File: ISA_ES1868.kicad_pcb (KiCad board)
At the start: 4 copper layers, 104.1 x 102.9 mm, 107 parts, among them J1 LINE IN, J10 Volume buttons, J11 ISA BUS, J2 MIC, J3 Joystick/MIDI, J5 Wavetable, J7 SPKR OUT, J8 LINE OUT, U1 L78L05, U2 74LS138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

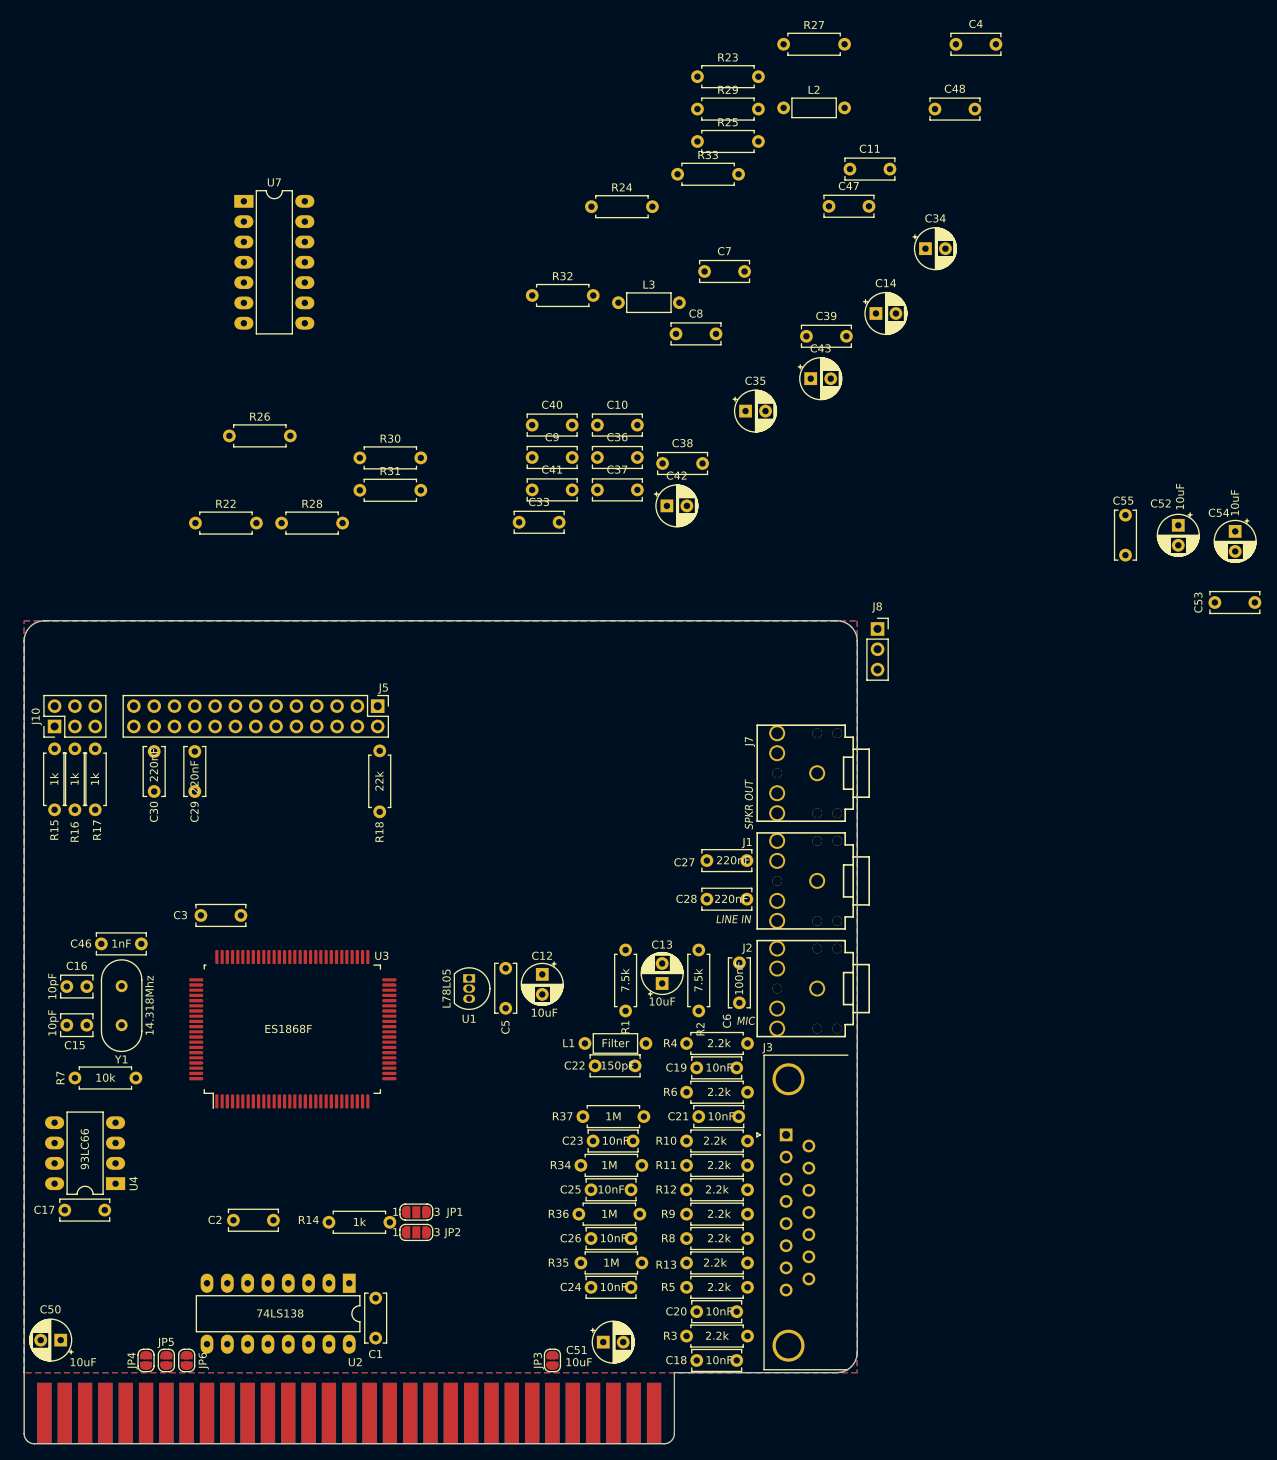
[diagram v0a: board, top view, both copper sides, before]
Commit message: Routed audio traces
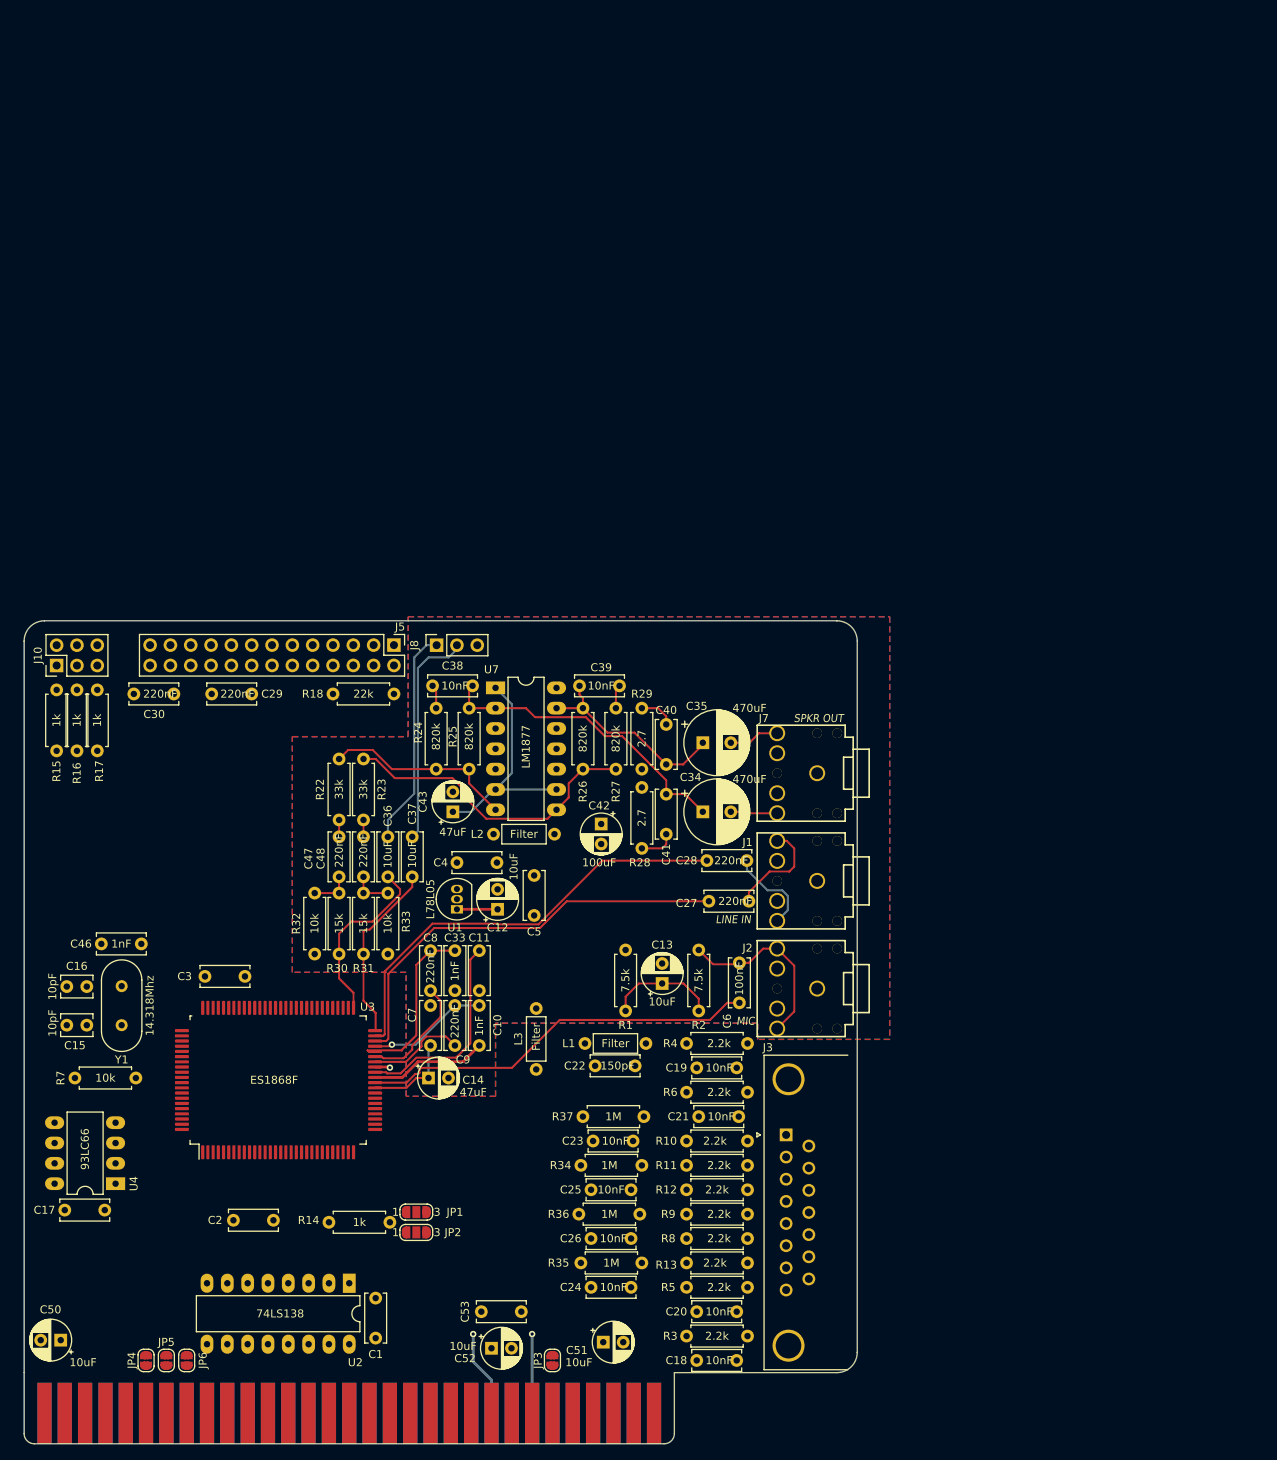
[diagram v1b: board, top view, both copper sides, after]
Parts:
- removed C54: 10uF, Capacitor_THT:CP_Radial_D5.0mm_P2.50mm
- removed C55: 100nF, Capacitor_THT:C_Disc_D6.0mm_W2.5mm_P5.00mm
- C34, C35: footprint Capacitor_THT:CP_Radial_D5.0mm_P2.50mm -> Capacitor_THT:CP_Radial_D8.0mm_P3.50mm
- L2, L3: value Ferrite Bead -> Filter
- moved C52 134.0 mm to (269.2, 191.3), turned to 0 degrees
- moved C53 127.5 mm to (268.0, 186.7)
- moved C4 119.8 mm to (264.9, 130.6)
- moved C48 119.6 mm to (253.2, 132.3), turned to 90 degrees
- moved C14 110.7 mm to (261.4, 157.5)
- moved C11 108.1 mm to (267.7, 141.6), turned to 270 degrees
- moved C47 103.8 mm to (250.2, 132.3), turned to 90 degrees
- moved C7 102.6 mm to (261.6, 153.4), turned to 90 degrees
- moved R23 101.9 mm to (253.2, 125.2), turned to 90 degrees
- moved L2 97.8 mm to (269.5, 127.0)
- moved R33 96.9 mm to (256.3, 134.4), turned to 270 degrees
- moved L3 96.4 mm to (274.8, 156.4), turned to 90 degrees
- moved R27 93.0 mm to (284.8, 118.9), turned to 90 degrees
- moved C8 87.6 mm to (261.6, 146.6), turned to 90 degrees
- moved R25 83.5 mm to (266.4, 118.9), turned to 90 degrees
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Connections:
- net Net-(C42-Pad1) renamed /Filtered_12V
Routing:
- net GNDA: track 0.00 -> 309.9 mm
- net +12V: track 0.00 -> 127.1 mm, vias 0 -> 1
- net Net-(C28-Pad1): track 0.00 -> 55.2 mm
- net Net-(C27-Pad1): track 0.00 -> 53.7 mm
- net Net-(C6-Pad1): track 0.00 -> 49.9 mm
- net /VDDA: track 0.00 -> 49.5 mm, vias 0 -> 1
- net Net-(R23-Pad2): track 0.00 -> 38.8 mm
- net Net-(C34-Pad1): track 0.00 -> 38.6 mm
- net Net-(C43-Pad1): track 0.00 -> 28.5 mm
- net Net-(C37-Pad2): track 0.00 -> 27.8 mm
- net Net-(C36-Pad2): track 0.00 -> 27.2 mm
- net /Filtered_12V: track 0.00 -> 27.2 mm
- net Net-(C11-Pad1): track 0.00 -> 26.4 mm
- net Net-(C35-Pad1): track 0.00 -> 25.4 mm
- net Net-(R22-Pad2): track 0.00 -> 24.2 mm
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- added copper zone on In2.Cu, net /VDDA
- added copper zone on B.Cu, net GNDA
- added copper zone on F.Cu, net GNDA
- added copper zone on In1.Cu, net GNDA
- removed copper zone on B.Cu, net GND
- removed copper zone on F.Cu, net GND

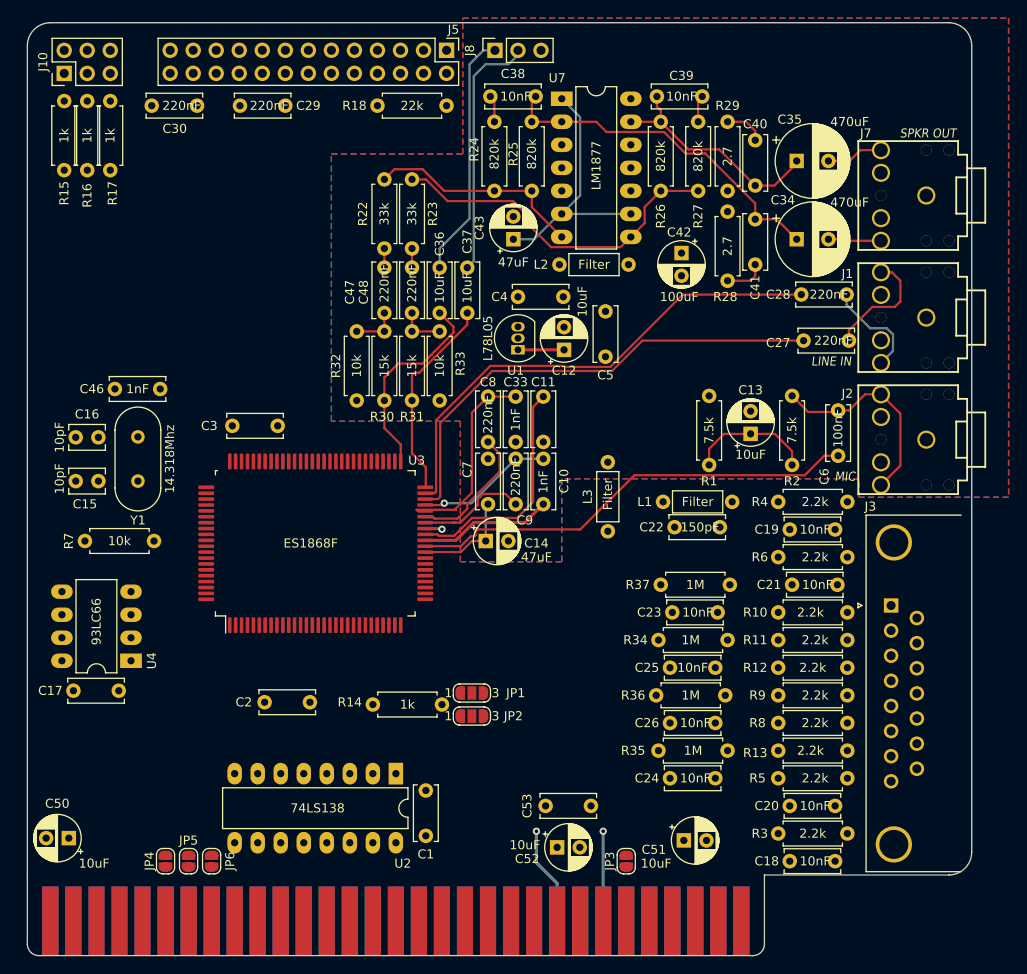
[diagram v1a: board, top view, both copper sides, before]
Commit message: Basic power routing
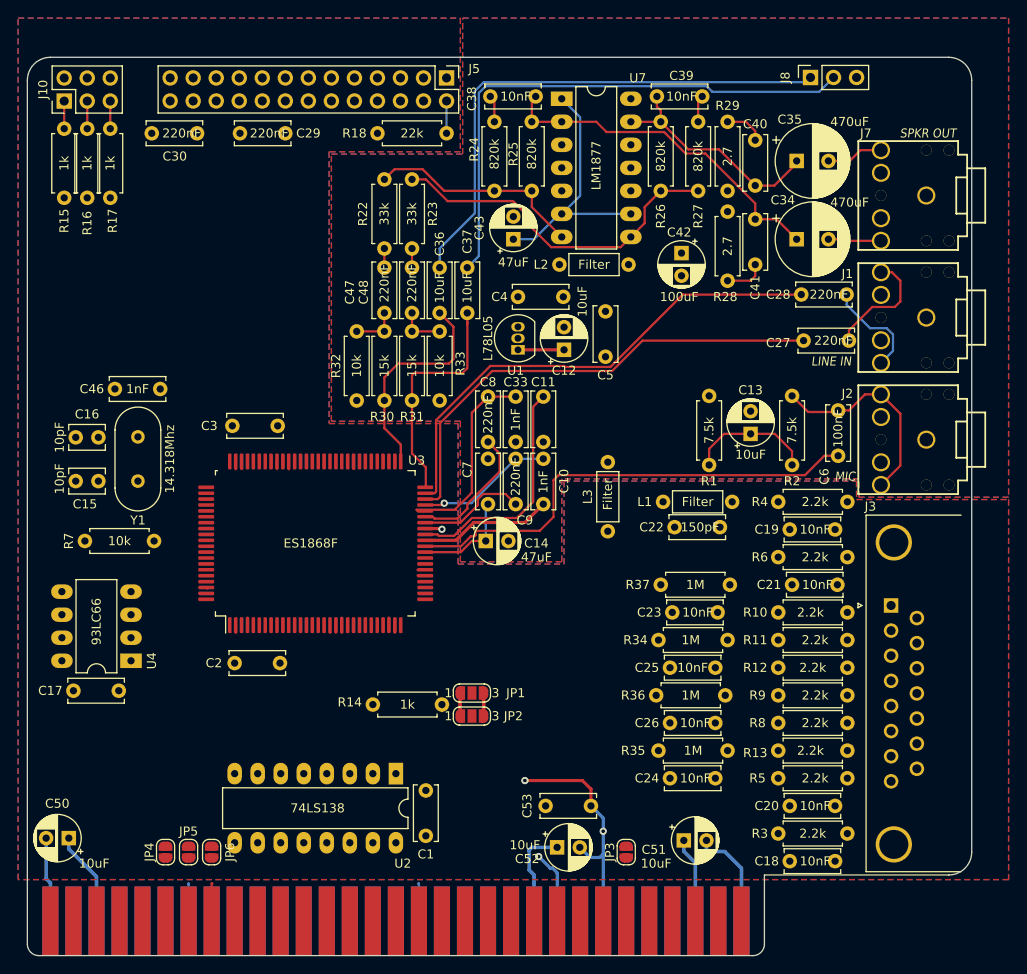
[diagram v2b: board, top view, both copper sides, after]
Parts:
- moved J8 34.9 mm to (297.2, 106.4)
- moved C2 5.44 mm to (233.7, 170.9)
- moved C29 3.05 mm to (239.3, 112.5)
- moved C30 3.05 mm to (224.5, 112.5)
- moved J5 3.05 mm to (257.0, 106.4)
- moved R15 3.05 mm to (214.9, 119.6)
- moved R16 3.05 mm to (217.4, 119.6)
- moved R17 3.05 mm to (220.0, 119.6)
- moved R18 3.05 mm to (257.0, 112.5)
- moved J10 3.05 mm to (214.9, 109.0)
- moved JP3 1.00 mm to (276.9, 191.8)
- moved JP4 1.00 mm to (226.1, 191.8)
- moved JP5 1.00 mm to (228.6, 191.8)
- moved JP6 1.00 mm to (231.1, 191.8)
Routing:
- net GND: track 0.00 -> 446.0 mm
- net VCC: track 0.00 -> 315.0 mm
- net -12V: track 9.91 -> 148.1 mm, vias 1 -> 2
- net Net-(C37-Pad2): track 27.8 -> 60.1 mm
- net Net-(C36-Pad2): track 27.2 -> 58.7 mm
- net GNDA: track 309.9 -> 296.6 mm
- net /IRQ3: track 0.00 -> 4.28 mm
- net /~DACK3: track 0.00 -> 4.24 mm
- net /A7: track 0.00 -> 4.23 mm
- net /MCLK: track 0.00 -> 3.57 mm
- net /AOUTL: track 22.7 -> 25.8 mm
- net Net-(J10-Pad5): track 0.00 -> 3.05 mm
- net Net-(J10-Pad3): track 0.00 -> 3.05 mm
- net Net-(J10-Pad1): track 0.00 -> 3.05 mm
- net /~DACK1: track 0.00 -> 2.64 mm
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- added copper zone on B.Cu, net GND
- added copper zone on F.Cu, net GND
- added copper zone on In1.Cu, net GND
- added copper zone on In2.Cu, net VCC
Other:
- board size 104.1 x 102.9 mm -> 104.1 x 99.1 mm
- net class POWER: trace_width 0.6 -> 0.4

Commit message: Commit pre-autoroute
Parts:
- JP3, JP4, JP5, JP6: moved to B.Cu
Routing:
- net GND: track 446.0 -> 532.0 mm, vias 0 -> 3
- net VCC: track 315.0 -> 370.9 mm, vias 0 -> 2
- net /IRQ3: track 4.28 -> 0.00 mm
- net /AOUTR: track 24.2 -> 25.9 mm
- net /AOUTL: track 25.8 -> 24.9 mm

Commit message: Routed
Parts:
- J8: footprint Connector_PinSocket_2.54mm:PinSocket_1x03_P2.54mm_Vertical -> Connector_PinHeader_2.54mm:PinHeader_1x03_P2.54mm_Horizontal
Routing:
- net GND: track 532.0 -> 664.7 mm, vias 3 -> 17
- net /MSO: track 0.00 -> 107.3 mm, vias 0 -> 1
- net /RESETDRV: track 0.00 -> 106.8 mm
- net Net-(R15-Pad1): track 0.50 -> 87.3 mm, vias 0 -> 3
- net /IRQ9: track 0.00 -> 82.7 mm, vias 0 -> 1
- net Net-(C19-Pad2): track 0.00 -> 75.5 mm
- net Net-(R16-Pad1): track 0.00 -> 75.4 mm, vias 0 -> 1
- net /MCLK: track 3.57 -> 77.6 mm
- net Net-(C18-Pad2): track 0.33 -> 74.0 mm, vias 0 -> 2
- net /A11: track 0.18 -> 72.7 mm, vias 0 -> 2
- net /IRQ7: track 0.84 -> 73.0 mm, vias 0 -> 1
- net Net-(R17-Pad1): track 0.92 -> 73.0 mm, vias 0 -> 3
- net /A10: track 0.00 -> 69.8 mm, vias 0 -> 2
- net /~IOW: track 0.00 -> 69.0 mm, vias 0 -> 2
- net Net-(C30-Pad1): track 0.86 -> 68.2 mm, vias 0 -> 2
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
